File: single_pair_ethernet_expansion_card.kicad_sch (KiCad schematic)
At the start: 54 parts, among them IC1 DP83TC813RRHFRQ1, J1 Conn_01x02, P1 USB_C_Plug, U1 LAN7801_9JX, U2 LP38693SD-3.3, U3 HD3SS3220IRNHT, U4 KC2520Z125.000C1KX00, U5 KC2520Z25.0000C1KX00

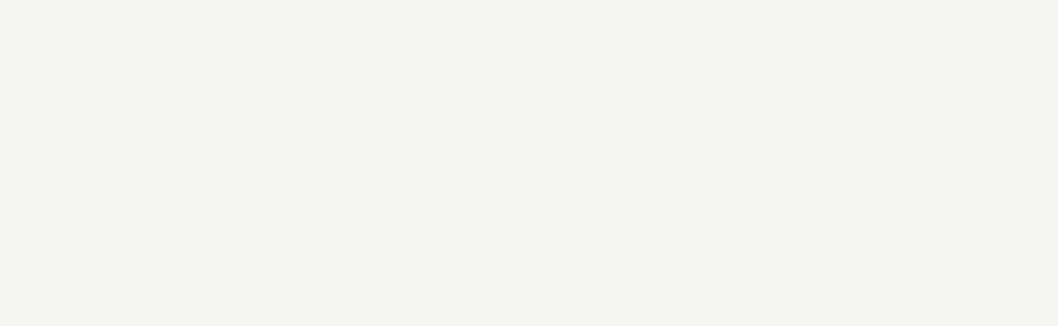
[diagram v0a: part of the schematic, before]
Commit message: fixed impedence
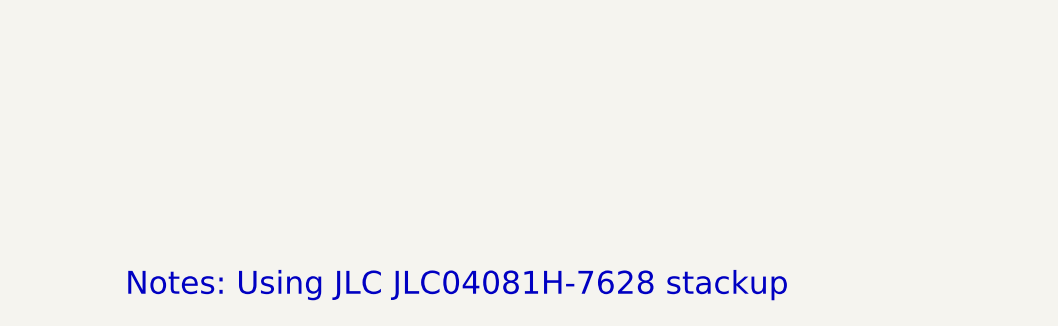
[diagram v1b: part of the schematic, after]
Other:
- note added: "Notes: Using JLC JLC04081H-7628 stackup"
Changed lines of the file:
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@@
+		)
+	)
+	(text "Notes: Using JLC JLC04081H-7628 stackup"
+		(exclude_from_sim no)
+		(at 56.896 280.67 0)
+		(effects
+			(font
+				(size 2.54 2.54)
+			)
 		)
 	)
